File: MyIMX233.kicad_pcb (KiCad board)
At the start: 2 copper layers, 74.5 x 112 mm, 40 parts, among them IC1 iMX233, IC2 DDR_SDRAM_MT46_x16, J1 USB_A, J2 Micro_SD_Card, SW1 SWITCH_PUSHBUTTON, Y1 24Mhz

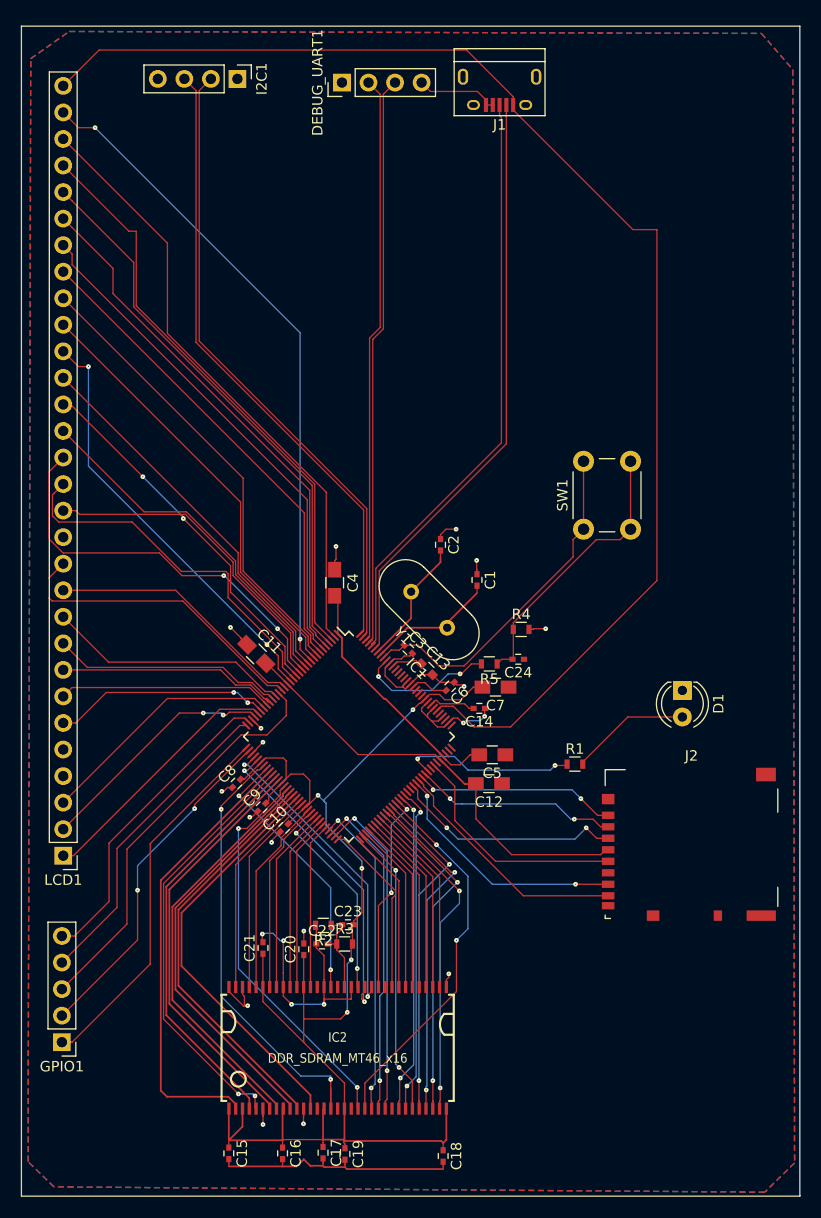
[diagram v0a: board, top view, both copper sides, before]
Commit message: lane 1 length matched 42.4
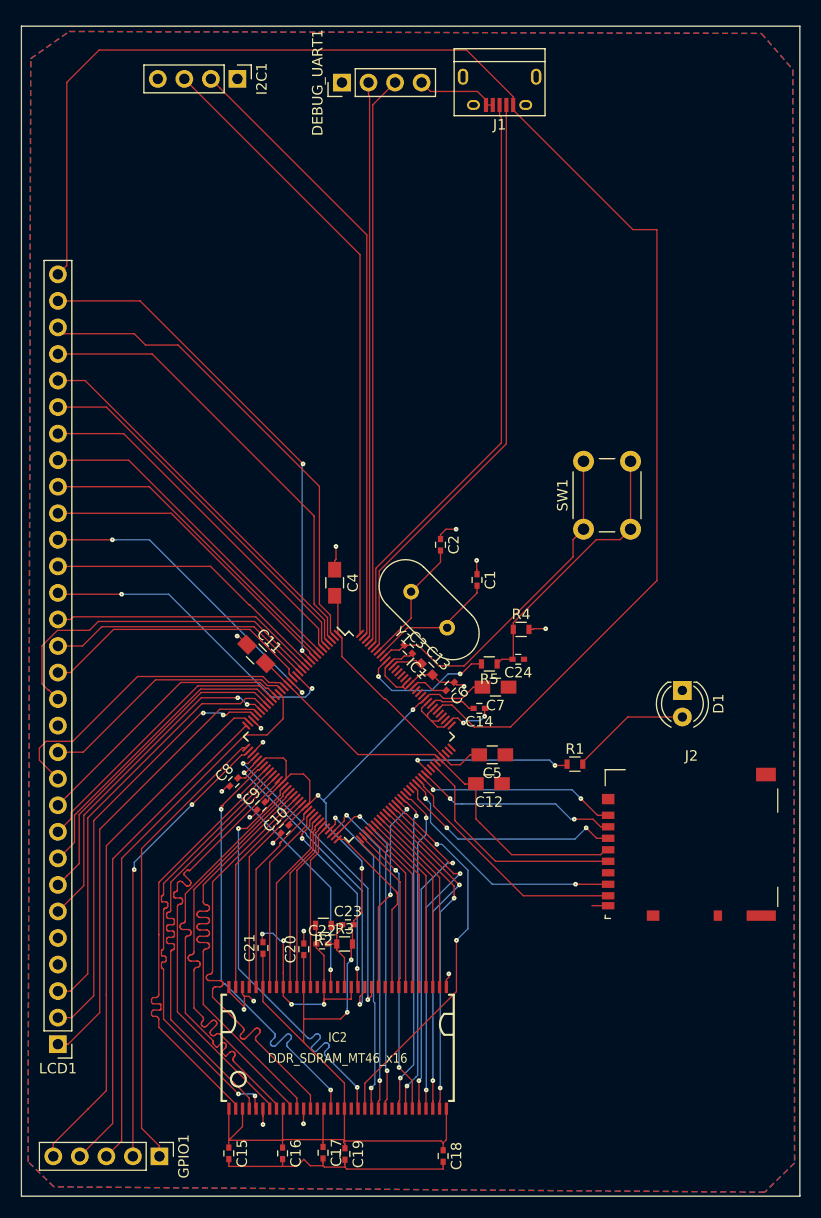
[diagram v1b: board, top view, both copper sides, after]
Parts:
- moved LCD1 18.0 mm to (69.2, 128.3)
- moved GPIO1 14.4 mm to (78.9, 139.1), turned to 270 degrees
- moved C8 0.28 mm to (86.0, 103.3)
- moved C10 0.14 mm to (90.9, 107.8)
- moved C9 0.14 mm to (88.6, 105.5)
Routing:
- net Net-(GPIO1-Pad5): track 30.0 -> 50.9 mm
- net +5V: track 127.5 -> 145.9 mm
- net Net-(IC1-Pad28): track 24.6 -> 42.9 mm
- net Net-(IC1-Pad29): track 23.3 -> 41.1 mm
- net Net-(GPIO1-Pad4): track 30.3 -> 47.8 mm
- net Net-(IC1-Pad26): track 23.7 -> 40.4 mm
- net Net-(IC1-Pad4): track 53.7 -> 37.4 mm
- net Net-(IC1-Pad5): track 51.3 -> 36.2 mm
- net Net-(IC1-Pad10): track 63.2 -> 49.2 mm, vias 3 -> 2
- net Net-(IC1-Pad6): track 48.7 -> 34.8 mm
- net Net-(IC1-Pad7): track 46.5 -> 32.7 mm
- net Net-(GPIO1-Pad3): track 39.0 -> 52.7 mm
- net Net-(IC1-Pad14): track 38.8 -> 25.7 mm, vias 2 -> 0
- net Net-(IC1-Pad3): track 56.4 -> 43.5 mm
- net Net-(IC1-Pad2): track 58.4 -> 46.3 mm
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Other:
- net class Default: clearance 0.12 -> 0.127; trace_width 0.12 -> 0.127
- rule trace_clearance: 0.12 -> 0.127
- rule trace_min: 0.1 -> 0.127

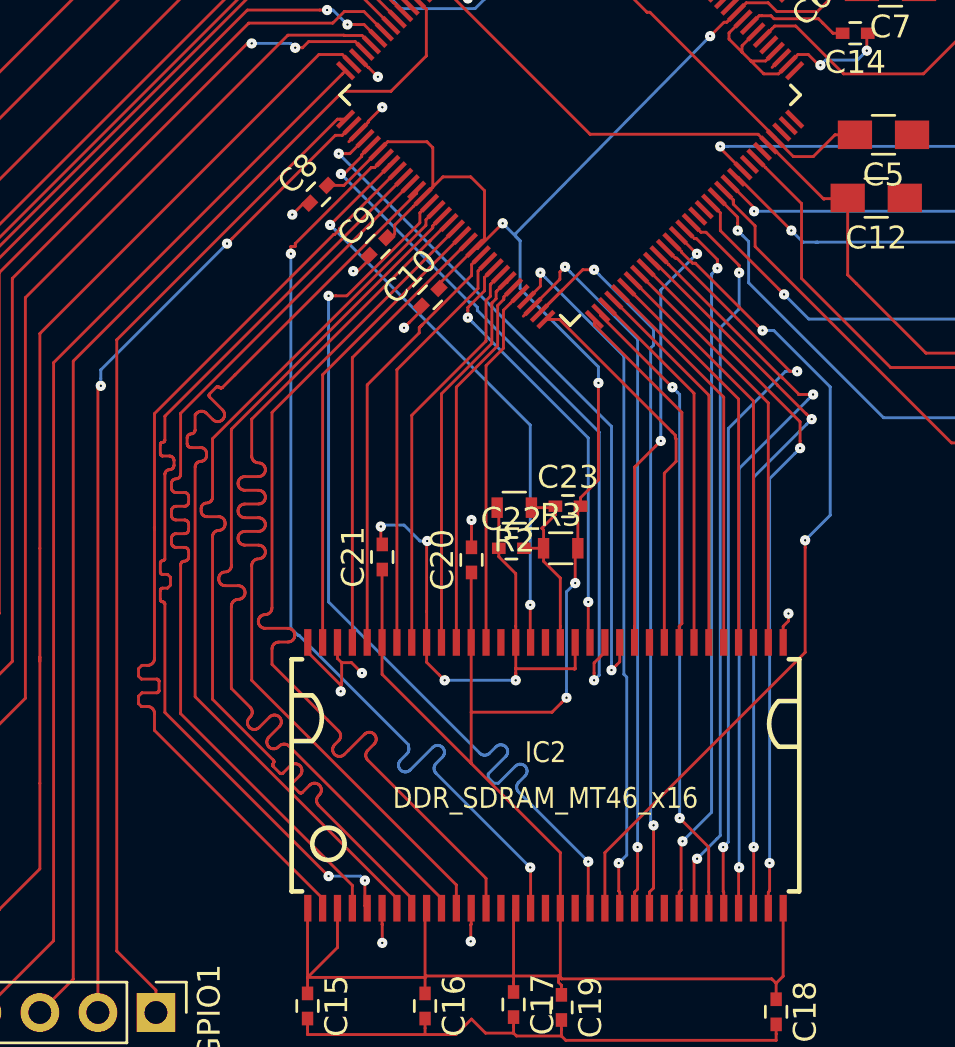
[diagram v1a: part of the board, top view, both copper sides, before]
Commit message: refs added plus tuned lengths of d8..15 and addr
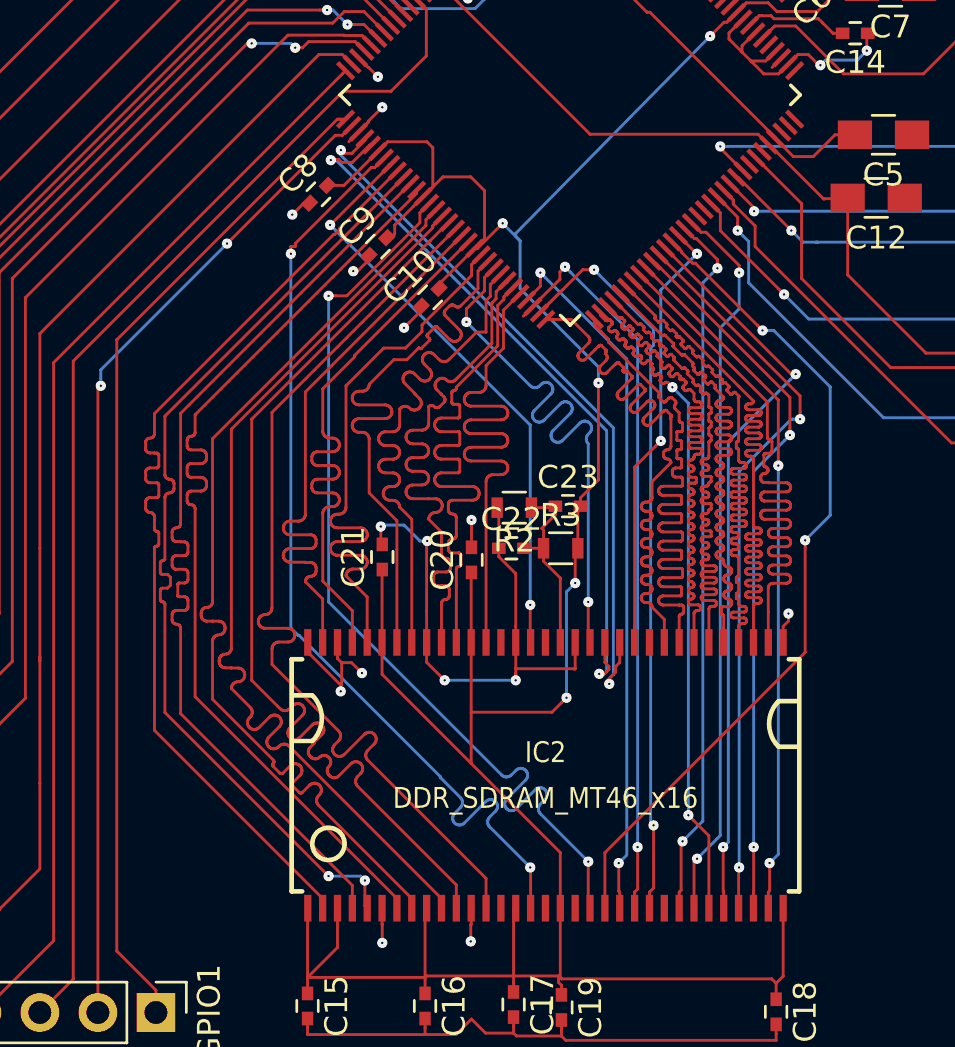
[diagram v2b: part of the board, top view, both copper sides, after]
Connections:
- net Net-(C22-Pad2) renamed /VREF
- net Net-(IC1-Pad36) renamed /CK+
- net Net-(IC1-Pad37) renamed /CK-
- net Net-(IC1-Pad39) renamed /LDQS
- net Net-(IC1-Pad40) renamed /UDQS
- net Net-(IC1-Pad46) renamed /LDM
- net Net-(IC1-Pad56) renamed /UDM
- net Net-(IC1-Pad61) renamed /CAS
- net Net-(IC1-Pad62) renamed /RAS
- net Net-(IC1-Pad63) renamed /CS
- net Net-(IC1-Pad77) renamed /WE
- net Net-(IC1-Pad78) renamed /CKE
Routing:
- net /A11: track 15.8 -> 30.5 mm
- net /A12: track 17.1 -> 30.6 mm
- net /A5: track 18.0 -> 30.5 mm
- net /A4: track 18.4 -> 30.5 mm
- net /A9: track 16.3 -> 28.3 mm
- net /A6: track 17.6 -> 29.0 mm
- net /A8: track 16.7 -> 27.0 mm
- net /A7: track 17.1 -> 27.1 mm
- net /D14: track 15.9 -> 25.6 mm
- net /D15: track 16.6 -> 25.4 mm
- net /D13: track 17.1 -> 25.6 mm
- net /D11: track 18.3 -> 26.1 mm
- net /D12: track 17.7 -> 25.5 mm
- net /UDM: track 19.1 -> 25.5 mm
- net /D10: track 19.2 -> 25.5 mm
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
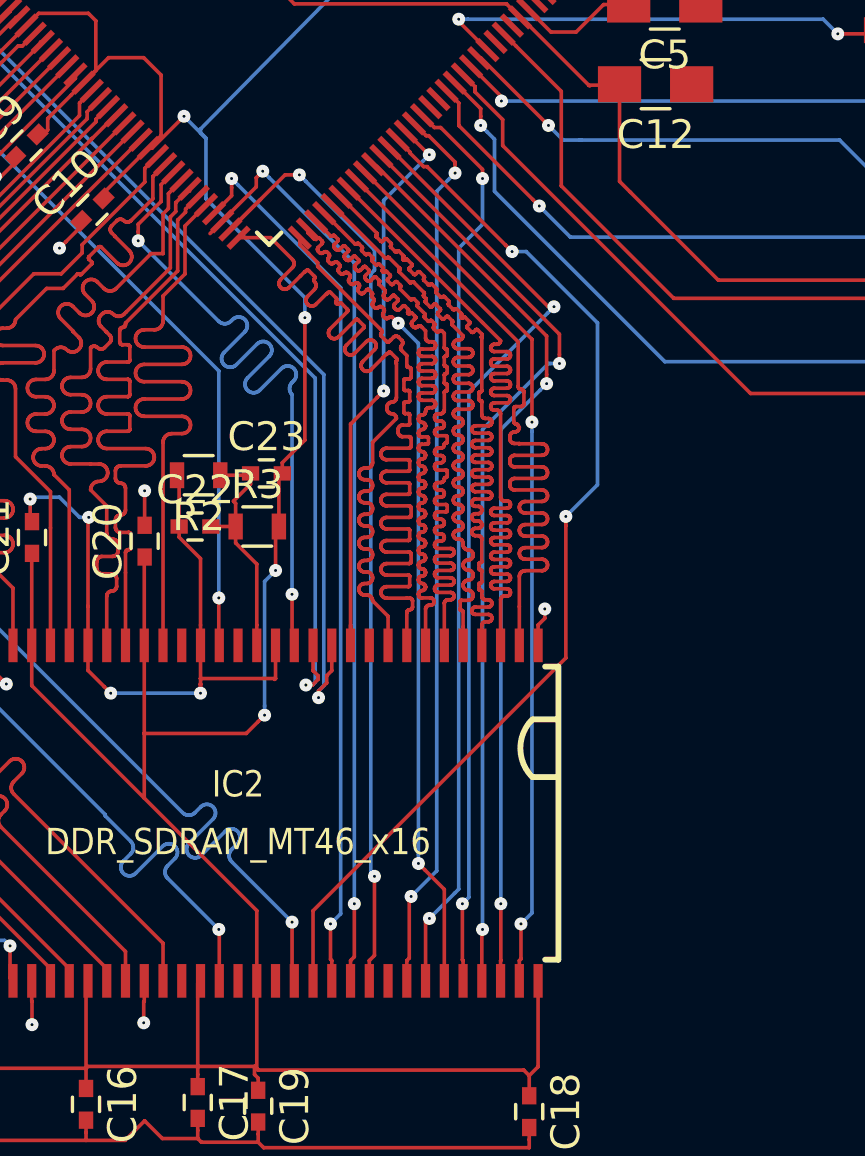
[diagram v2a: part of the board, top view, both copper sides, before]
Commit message: updated pcb export with 3d step files plus my new DDR step and FreeCAD proj
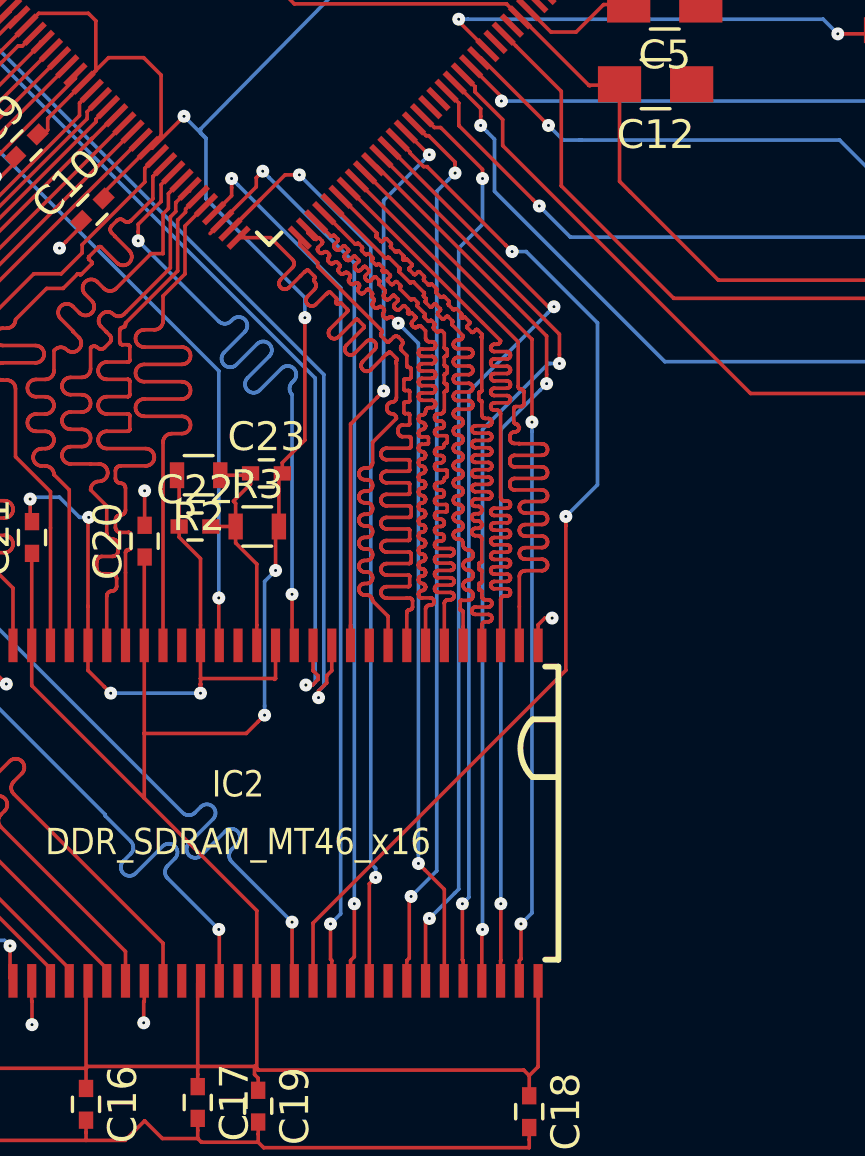
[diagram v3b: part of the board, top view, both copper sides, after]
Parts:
- IC2: footprint opendous:TSOP66_JEDEC_DDR_SDRAM -> mylib:TSOP66_JEDEC_DDR_SDRAM
- J1: footprint Connectors:USB_Micro-B -> mylib:USB_Micro-B_MOLEX_105017-0001
- J2: footprint Connectors_Hirose:microSD_Card_Receptacle_Hirose_DM3AT-SF-PEJM5 -> mylib:microSD_Card_Receptacle_Hirose_DM3AT-SF-PEJM5

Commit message: before dcdc
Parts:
- IC2: footprint mylib:TSOP66_JEDEC_DDR_SDRAM -> opendous:TSOP66_JEDEC_DDR_SDRAM
- moved J1 20.2 mm to (118.6, 56.0)
- moved I2C1 17.4 mm to (87.6, 53.3)
- moved DEBUG_UART1 17.3 mm to (99.2, 53.3)
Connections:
- net Net-(IC1-Pad83) renamed /SD_CMD
- net Net-(IC1-Pad84) renamed /SD0
- net Net-(IC1-Pad85) renamed /SD1
- net Net-(IC1-Pad86) renamed /SD2
- net Net-(IC1-Pad87) renamed /SD3
- net Net-(IC1-Pad90) renamed /SD_CLK
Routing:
- net +5V: track 145.9 -> 127.1 mm
- net /AUART+: track 60.1 -> 42.2 mm
- net /AUART-: track 59.7 -> 42.7 mm
- net /D-: track 57.2 -> 41.3 mm
- net /D+: track 57.0 -> 41.1 mm
- net /DUART+: track 54.6 -> 38.8 mm
- net /DUART-: track 53.5 -> 38.6 mm
- net /SD3: track 19.7 -> 30.5 mm
- net GND: track 111.1 -> 107.1 mm
- net /SD2: track 19.4 -> 22.7 mm
- net /SD0: track 23.8 -> 22.7 mm
- net /SD1: track 23.4 -> 22.7 mm
- net /SD_CMD: track 22.1 -> 22.7 mm
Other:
- board size 74.5 x 112 mm -> 74.1 x 92 mm
